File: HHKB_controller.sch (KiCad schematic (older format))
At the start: 32 parts, among them CN1 CONN_15, CN2 CONN_13, J1 USB_mini_micro_B, P1 GND, P2 D+, P3 D-, P4 VUSB, P5 PD1, P6 PD0, P7 GND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

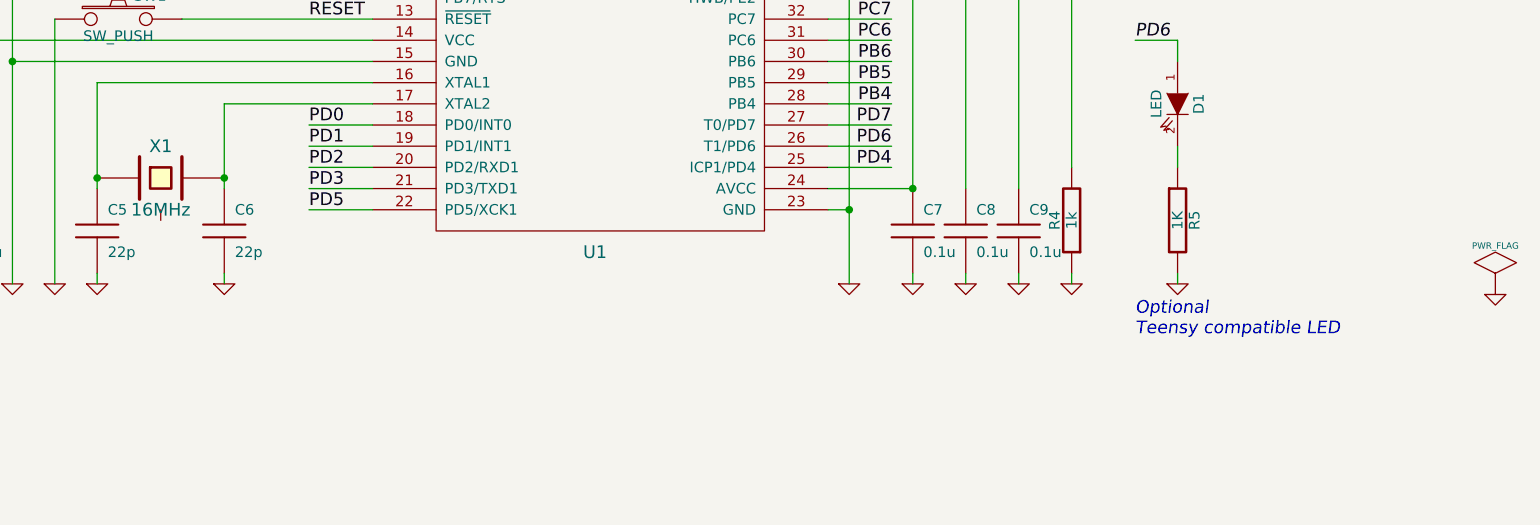
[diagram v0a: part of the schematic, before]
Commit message: Change schematic for dual LEDs
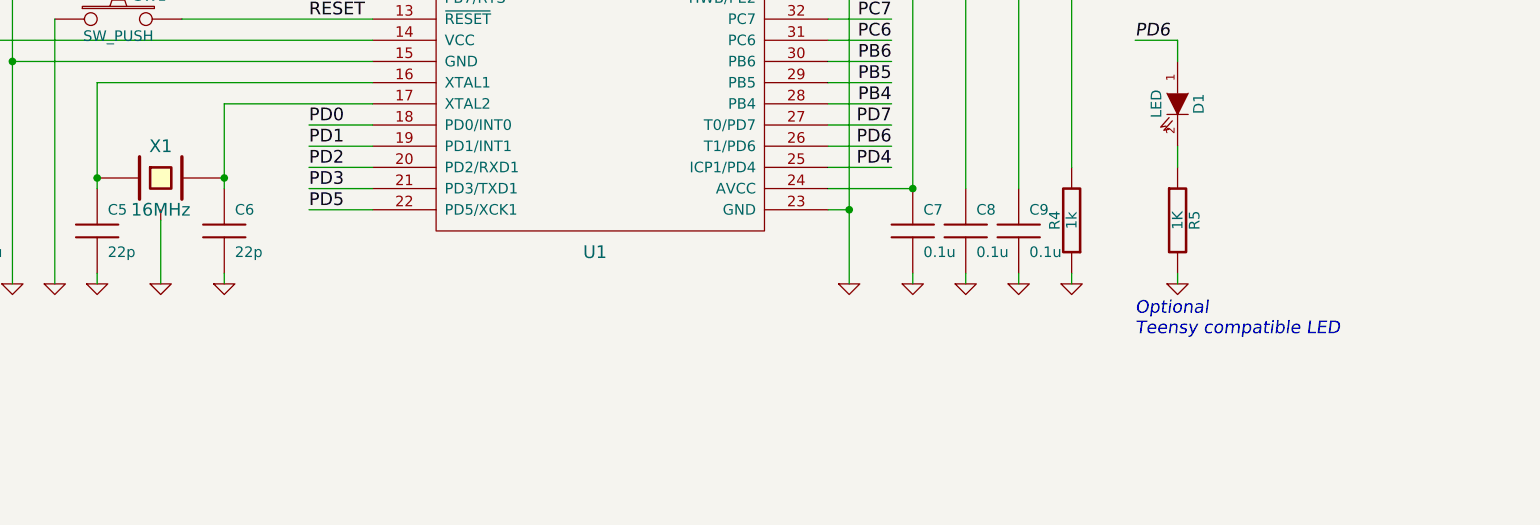
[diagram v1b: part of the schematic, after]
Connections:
- wire segments 147 -> 148
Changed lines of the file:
@@
 Sheet 1 2
 Title "HHKB Alt Controller/Bluetooth"
-Date "2014/07"
-Rev "C"
+Date "2014/09"
+Rev "D"
 Comp "TMK"
 Comment1 ""
@@
 	1    0    0    -1
 $EndComp
-$Comp
-L GND #PWR025
-U 1 1 4EBBEF66
-P 10950 3900
-F 0 "#PWR025" H 10950 3900 30  0001 C CNN
-F 1 "GND" H 10950 3830 30  0001 C CNN
-F 2 "" H 10950 3900 60  0001 C CNN
-F 3 "" H 10950 3900 60  0001 C CNN
-	1    10950 3900
-	1    0    0    -1
-$EndComp
-$Comp
-L PWR_FLAG #FLG026
-U 1 1 4EBBEFCE
-P 10950 3900
-F 0 "#FLG026" H 10950 4170 30  0001 C CNN
-F 1 "PWR_FLAG" H 10950 4130 30  0000 C CNN
-F 2 "" H 10950 3900 60  0001 C CNN
-F 3 "" H 10950 3900 60  0001 C CNN
-	1    10950 3900
-	1    0    0    -1
-$EndComp
 Text GLabel 6650 6050 2    60   Input ~ 0
 BT_CTS
@@
 Text Notes 1175 4025 0    60   ~ 0
 5V Power Source Select
+Wire Wire Line
+	4650 3550 4650 3850
+$Comp
+L GND #PWR025
+U 1 1 540DEB0D
+P 4650 3850
+F 0 "#PWR025" H 4650 3850 30  0001 C CNN
+F 1 "GND" H 4650 3780 30  0001 C CNN
+F 2 "" H 4650 3850 60  0001 C CNN
+F 3 "" H 4650 3850 60  0001 C CNN
+	1    4650 3850
+	1    0    0    -1
+$EndComp
 $EndSCHEMATC

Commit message: Final fixes for Rev.D
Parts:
- added JP1: JUMPER, keyboard_parts:SOLDER_JUMPER_2, symbol JUMPER
- added PPTC1: PPTC, keyboard_parts:PPTC_nano, symbol PPTC
- C1: value 10u -> 4.7u; footprint (none) -> keyboard_parts:C_3216
- C10, C3, C4, C5, C6, C7, C8, C9: footprint (none) -> keyboard_parts:C_1608
- CN1: value CONN_15 -> JP; footprint (none) -> keyboard_parts:HHKB_JP_HRS_DF14_15P
- CN2: value CONN_13 -> PRO2; footprint (none) -> keyboard_parts:HHKB_PRO2_ZH13
- D1: footprint (none) -> keyboard_parts:LED_2012_HSOL
- J1: footprint (none) -> keyboard_parts:USB_miniB_hirose_new
- JP2, JP3: footprint (none) -> keyboard_parts:SOLDER_JUMPER_2
- P1, P2, P3, P5, P6, P7: footprint (none) -> keyboard_parts:PIN_1
- P4: footprint (none) -> keyboard_parts:PIN_1_SQUARE
- P8: footprint (none) -> keyboard_parts:AVR_ICSP_3x2
- Q2: value MOSFET_N -> MOS_N; footprint (none) -> keyboard_parts:MOS_FET_SOT23-3_HSOL
- R15, R2, R3, R4, R5: footprint (none) -> keyboard_parts:R_1608
- SW1: footprint (none) -> keyboard_parts:SW_TACT_TH_HORIZ_LOW
- U1: footprint (none) -> keyboard_parts:QFP44
- X1: footprint (none) -> keyboard_parts:HC-49_SMT
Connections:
- net labels added: ADC_CTRL, ADC_LIPO, VUSB_RAW
- net labels removed: LIPO_SENSE
- wire segments 148 -> 154
- no-connect marks 2 -> 1
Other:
- note added: "No PPTC"
- moved on the sheet: R2, R3

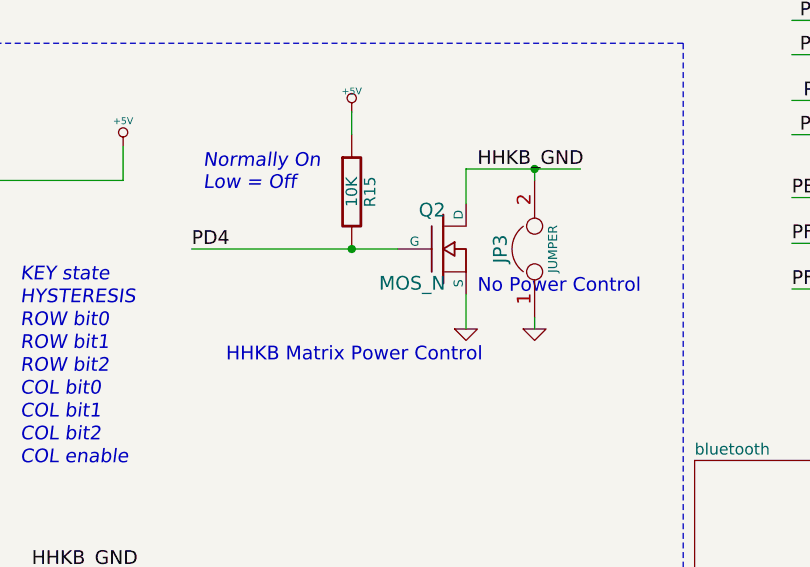
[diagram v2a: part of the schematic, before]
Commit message: Add D5 schottky and change C15 size and C14 value
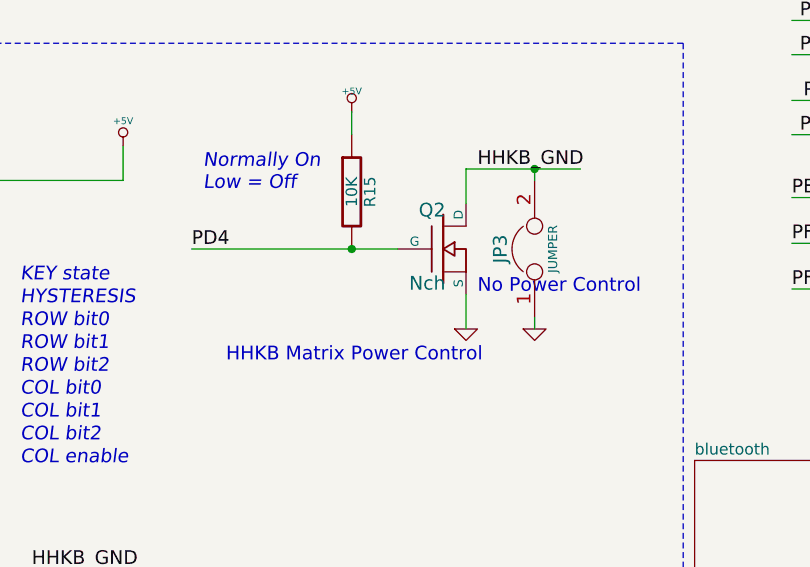
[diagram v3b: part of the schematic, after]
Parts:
- Q2: value MOS_N -> Nch
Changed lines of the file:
@@
 P 4675 5900
 F 0 "Q2" H 4685 6070 60  0000 R CNN
-F 1 "MOS_N" H 4685 5750 60  0000 R CNN
+F 1 "Nch" H 4685 5750 60  0000 R CNN
 F 2 "keyboard_parts:MOS_FET_SOT23-3_HSOL" H 4675 5900 60  0001 C CNN
 F 3 "" H 4675 5900 60  0000 C CNN

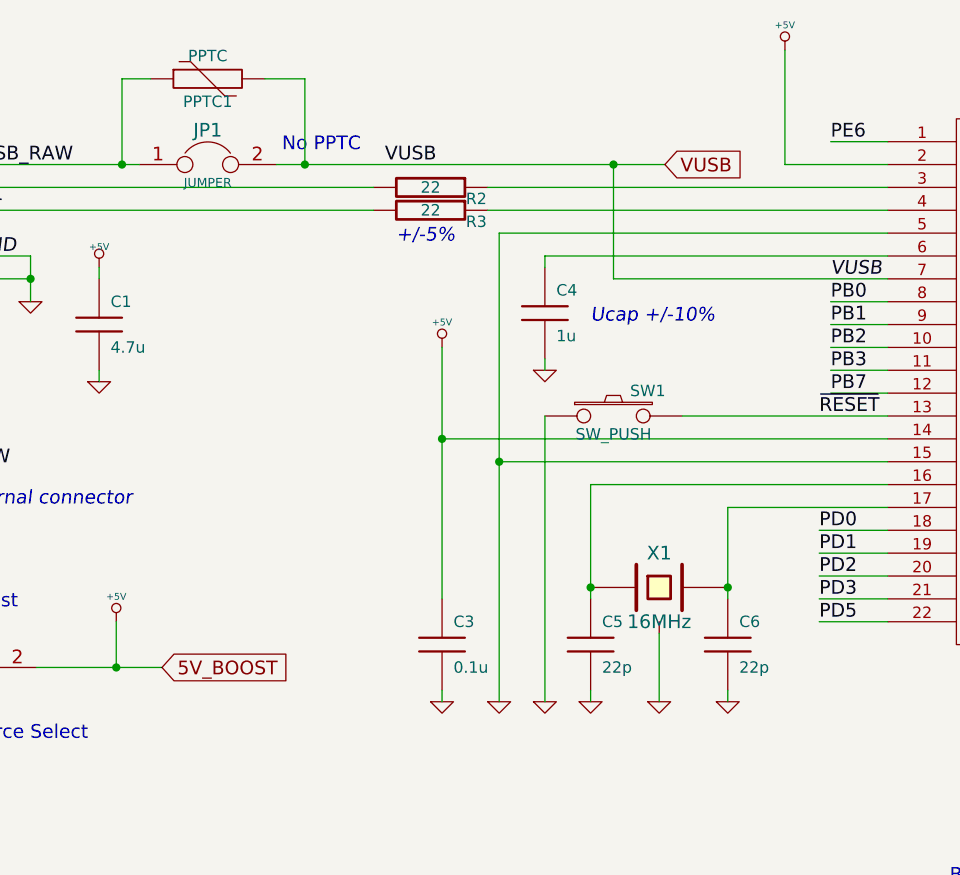
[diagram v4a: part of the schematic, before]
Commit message: Fix UVCC
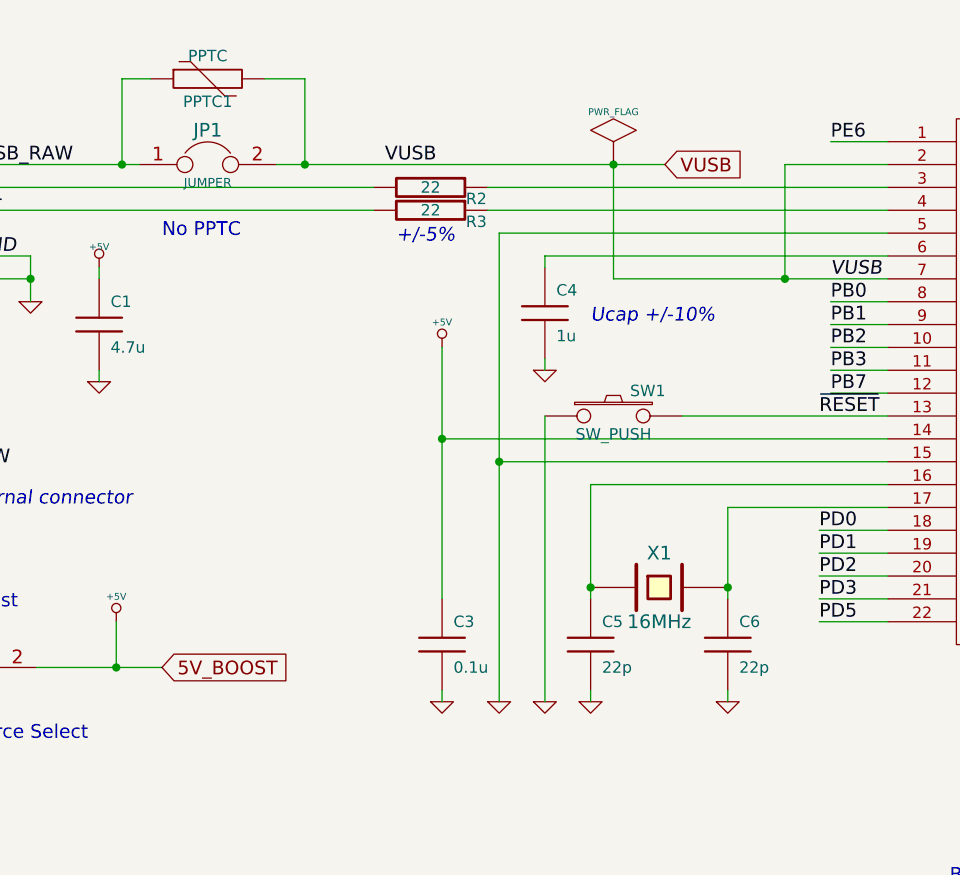
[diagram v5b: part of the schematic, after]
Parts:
- removed X1: 16MHz, keyboard_parts:HC-49_SMT, symbol CRYSTAL
- added X1: 16MHz, keyboard_parts:HC-49_SMT, symbol XTAL
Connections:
- wire segments 154 -> 153
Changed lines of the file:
@@
-	1    0    0    -1
-$EndComp
-$Comp
-L CRYSTAL X1
-U 1 1 4EB8BB56
-P 4650 3350
-F 0 "X1" H 4650 3500 60  0000 C CNN
-F 1 "16MHz" H 4650 3200 60  0000 C CNN
-F 2 "keyboard_parts:HC-49_SMT" H 4650 3350 60  0001 C CNN
-F 3 "" H 4650 3350 60  0001 C CNN
-	1    4650 3350
 	1    0    0    -1
 $EndComp
@@
 Text Notes 625  7550 0    60   Italic 0
 Hirose DF14A for JP
-$Comp
-L +5V #PWR018
-U 1 1 519EBD1D
-P 5200 1000
-F 0 "#PWR018" H 5200 970 20  0001 C CNN
-F 1 "+5V" H 5200 1110 30  0000 C CNN
-F 2 "" H 5200 1000 60  0001 C CNN
-F 3 "" H 5200 1000 60  0001 C CNN
-	1    5200 1000
-	1    0    0    -1
-$EndComp
 Text Label 5400 2000 0    60   Italic 0
 VUSB
@@
 GND
 $Comp
-L GND #PWR019
+L GND #PWR018
 U 1 1 51A7FC37
 P 2200 2450
-F 0 "#PWR019" H 2200 2450 30  0001 C CNN
+F 0 "#PWR018" H 2200 2450 30  0001 C CNN
 F 1 "GND" H 2200 2380 30  0001 C CNN
 F 2 "" H 2200 2450 60  0000 C CNN
@@
 $EndComp
 $Comp
-L +5V #PWR020
+L +5V #PWR019
 U 1 1 51A7FC46
 P 2200 1950
-F 0 "#PWR020" H 2200 2040 20  0001 C CNN
+F 0 "#PWR019" H 2200 2040 20  0001 C CNN
 F 1 "+5V" H 2200 2040 30  0000 C CNN
 F 2 "" H 2200 1950 60  0000 C CNN
@@
 $EndComp
 $Comp
-L GND #PWR021
+L GND #PWR020
 U 1 1 51AD5139
 P 9450 2200
-F 0 "#PWR021" H 9450 2200 30  0001 C CNN
+F 0 "#PWR020" H 9450 2200 30  0001 C CNN
 F 1 "GND" H 9450 2130 30  0001 C CNN
 F 2 "" H 9450 2200 60  0000 C CNN
@@
 $EndComp
 $Comp
-L GND #PWR022
+L GND #PWR021
 U 1 1 51BB4B45
 P 4775 6250
-F 0 "#PWR022" H 4775 6250 30  0001 C CNN
+F 0 "#PWR021" H 4775 6250 30  0001 C CNN
 F 1 "GND" H 4775 6180 30  0001 C CNN
 F 2 "" H 4775 6250 60  0000 C CNN
@@
 $EndComp
 $Comp
-L +5V #PWR023
+L +5V #PWR022
 U 1 1 51BB4C0E
 P 4275 5300
-F 0 "#PWR023" H 4275 5390 20  0001 C CNN
+F 0 "#PWR022" H 4275 5390 20  0001 C CNN
 F 1 "+5V" H 4275 5390 30  0000 C CNN
 F 2 "" H 4275 5300 60  0000 C CNN
@@
 PF0
 $Comp
-L GND #PWR024
+L GND #PWR023
 U 1 1 52AACE12
 P 5075 6250
-F 0 "#PWR024" H 5075 6250 30  0001 C CNN
+F 0 "#PWR023" H 5075 6250 30  0001 C CNN
 F 1 "GND" H 5075 6180 30  0001 C CNN
 F 2 "" H 5075 6250 60  0000 C CNN
@@
 Text Notes 9000 5150 0    60   ~ 0
 Program and Debug
+$Comp
+L USB_mini_micro_B J1
+U 1 1 53485EB0
+P 1450 1650
+F 0 "J1" H 1050 1600 60  0000 C CNN
+F 1 "USB_mini_micro_B" H 1300 1900 60  0001 C CNN
+F 2 "keyboard_parts:USB_miniB_hirose_new" H 1400 1650 60  0001 C CNN
+F 3 "" H 1400 1650 60  0000 C CNN
+	1    1450 1650
+	1    0    0    -1
+$EndComp
+Text GLabel 6600 5875 2    60   Input ~ 0
+BT_CONN
+Text Label 6200 5875 0    60   ~ 0
+PF7
+Text GLabel 6600 6075 2    60   Input ~ 0
+LINKED
+Text Label 6200 6075 0    60   ~ 0
+PF6
+Text GLabel 7675 5225 2    60   Input ~ 0
+~CHRG
+Text Label 7275 5225 0    60   ~ 0
+PF5
+Text Notes 3525 7600 0    60   Italic 0
+Optional
+Text Label 925  3700 0    60   ~ 0
+VUSB
+Text Notes 1175 4025 0    60   ~ 0
+5V Power Source Select
+Text GLabel 7675 5075 2    60   Input ~ 0
+ADC_CTRL
+Text Label 7275 5075 0    60   ~ 0
+PF4
+Text Notes 2475 1825 0    60   ~ 0
+No PPTC
+$Comp
+L PPTC PPTC1
+U 1 1 5417AF4F
+P 2675 1125
+F 0 "PPTC1" H 2675 1225 50  0000 C CNN
+F 1 "PPTC" H 2675 1025 50  0000 C CNN
+F 2 "keyboard_parts:PPTC_nano" V 2675 1125 60  0001 C CNN
+F 3 "" V 2675 1125 60  0000 C CNN
+	1    2675 1125
+	1    0    0    1
+$EndComp
+$Comp
+L JUMPER JP1
+U 1 1 5417AF56
+P 2675 1500
+F 0 "JP1" H 2675 1650 60  0000 C CNN
+F 1 "JUMPER" H 2675 1420 40  0000 C CNN
+F 2 "keyboard_parts:SOLDER_JUMPER_2" H 2675 1500 60  0001 C CNN
+F 3 "" H 2675 1500 60  0000 C CNN
+	1    2675 1500
+	1    0    0    -1
+$EndComp
+Text Label 3450 1500 0    60   ~ 0
+VUSB
 Wire Wire Line
 	1300 2825 1600 2825
@@
 Wire Wire Line
 	1225 7050 1425 7050
-Wire Wire Line
-	5200 1000 5200 1500
 Wire Wire Line
 	5200 1500 5650 1500
@@
 Wire Notes Line
 	8950 5000 11050 5000
-$Comp
-L USB_mini_micro_B J1
-U 1 1 53485EB0
-P 1450 1650
-F 0 "J1" H 1050 1600 60  0000 C CNN
-F 1 "USB_mini_micro_B" H 1300 1900 60  0001 C CNN
-F 2 "keyboard_parts:USB_miniB_hirose_new" H 1400 1650 60  0001 C CNN
-F 3 "" H 1400 1650 60  0000 C CNN
-	1    1450 1650
-	1    0    0    -1
-$EndComp
-Text GLabel 6600 5875 2    60   Input ~ 0
-BT_CONN
 Wire Wire Line
 	6600 5875 6200 5875
-Text Label 6200 5875 0    60   ~ 0
-PF7
 Wire Wire Line
 	6200 6075 6600 6075
-Text GLabel 6600 6075 2    60   Input ~ 0
-LINKED
-Text Label 6200 6075 0    60   ~ 0
-PF6
 Wire Wire Line
 	7275 5225 7675 5225
-Text GLabel 7675 5225 2    60   Input ~ 0
-~CHRG
-Text Label 7275 5225 0    60   ~ 0
-PF5
-Text Notes 3525 7600 0    60   Italic 0
-Optional
 Wire Wire Line
 	1425 5950 1425 5600
@@
 Wire Wire Line
 	1325 3700 925  3700
-Text Label 925  3700 0    60   ~ 0
-VUSB
-Text Notes 1175 4025 0    60   ~ 0
-5V Power Source Select
-Wire Wire Line
-	4650 3550 4650 3850
-$Comp
-L GND #PWR025
-U 1 1 540DEB0D
-P 4650 3850
-F 0 "#PWR025" H 4650 3850 30  0001 C CNN
-F 1 "GND" H 4650 3780 30  0001 C CNN
-F 2 "" H 4650 3850 60  0001 C CNN
-F 3 "" H 4650 3850 60  0001 C CNN
-	1    4650 3850
-	1    0    0    -1
-$EndComp
 Wire Wire Line
 	7275 5075 7675 5075
-Text GLabel 7675 5075 2    60   Input ~ 0
-ADC_CTRL
-Text Label 7275 5075 0    60   ~ 0
-PF4
-Text Notes 3000 1450 0    60   ~ 0
-No PPTC
-$Comp
-L PPTC PPTC1
-U 1 1 5417AF4F
-P 2675 1125
-F 0 "PPTC1" H 2675 1225 50  0000 C CNN
-F 1 "PPTC" H 2675 1025 50  0000 C CNN
-F 2 "keyboard_parts:PPTC_nano" V 2675 1125 60  0001 C CNN
-F 3 "" V 2675 1125 60  0000 C CNN
-	1    2675 1125
-	1    0    0    1
-$EndComp
-$Comp
-L JUMPER JP1
-U 1 1 5417AF56
-P 2675 1500
-F 0 "JP1" H 2675 1650 60  0000 C CNN
-F 1 "JUMPER" H 2675 1420 40  0000 C CNN
-F 2 "keyboard_parts:SOLDER_JUMPER_2" H 2675 1500 60  0001 C CNN
-F 3 "" H 2675 1500 60  0000 C CNN
-	1    2675 1500
-	1    0    0    -1
-$EndComp
 Wire Wire Line
 	3900 1600 5650 1600
@@
 	3100 1125 3100 1500
 Connection ~ 3100 1500
-Text Label 3450 1500 0    60   ~ 0
-VUSB
+Wire Wire Line
+	5200 1500 5200 2000
+Connection ~ 5200 2000
+$Comp
+L XTAL X1
+U 1 1 5453AC44
+P 4650 3350
+F 0 "X1" H 4650 3500 60  0000 C CNN
+F 1 "16MHz" H 4650 3200 60  0000 C CNN
+F 2 "keyboard_parts:HC-49_SMT" H 4650 3350 60  0001 C CNN
+F 3 "" H 4650 3350 60  0000 C CNN
+	1    4650 3350
+	1    0    0    -1
+$EndComp
+$Comp
+L PWR_FLAG #FLG024
+U 1 1 5453B6D9
+P 4450 1500
+F 0 "#FLG024" H 4450 1770 30  0001 C CNN
+F 1 "PWR_FLAG" H 4450 1730 30  0000 C CNN
+F 2 "" H 4450 1500 60  0000 C CNN
+F 3 "" H 4450 1500 60  0000 C CNN
+	1    4450 1500
+	1    0    0    -1
+$EndComp
 $EndSCHEMATC
